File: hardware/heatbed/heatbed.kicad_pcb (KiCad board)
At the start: 2 copper layers, 400 x 400 mm, 0 parts

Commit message: finish board and prod/case files
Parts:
- added J1: Conn_01x01, TestPoint:TestPoint_Pad_D4.0mm, F.Cu at (162.2, 250.3)
- added J2: Conn_01x01, TestPoint:TestPoint_Pad_D4.0mm, F.Cu at (172.3, 250.3)
- added R1: R, Resistor_SMD:R_0805_2012Metric, F.Cu at (167.3, 154.2)
- added R2: R, Resistor_SMD:R_0805_2012Metric, F.Cu at (167.3, 248.8)
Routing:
- net Net-(J1-Pin_1): track 6376.9 -> 0.00 mm
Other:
- board size 400 x 400 mm -> 200 x 200 mm

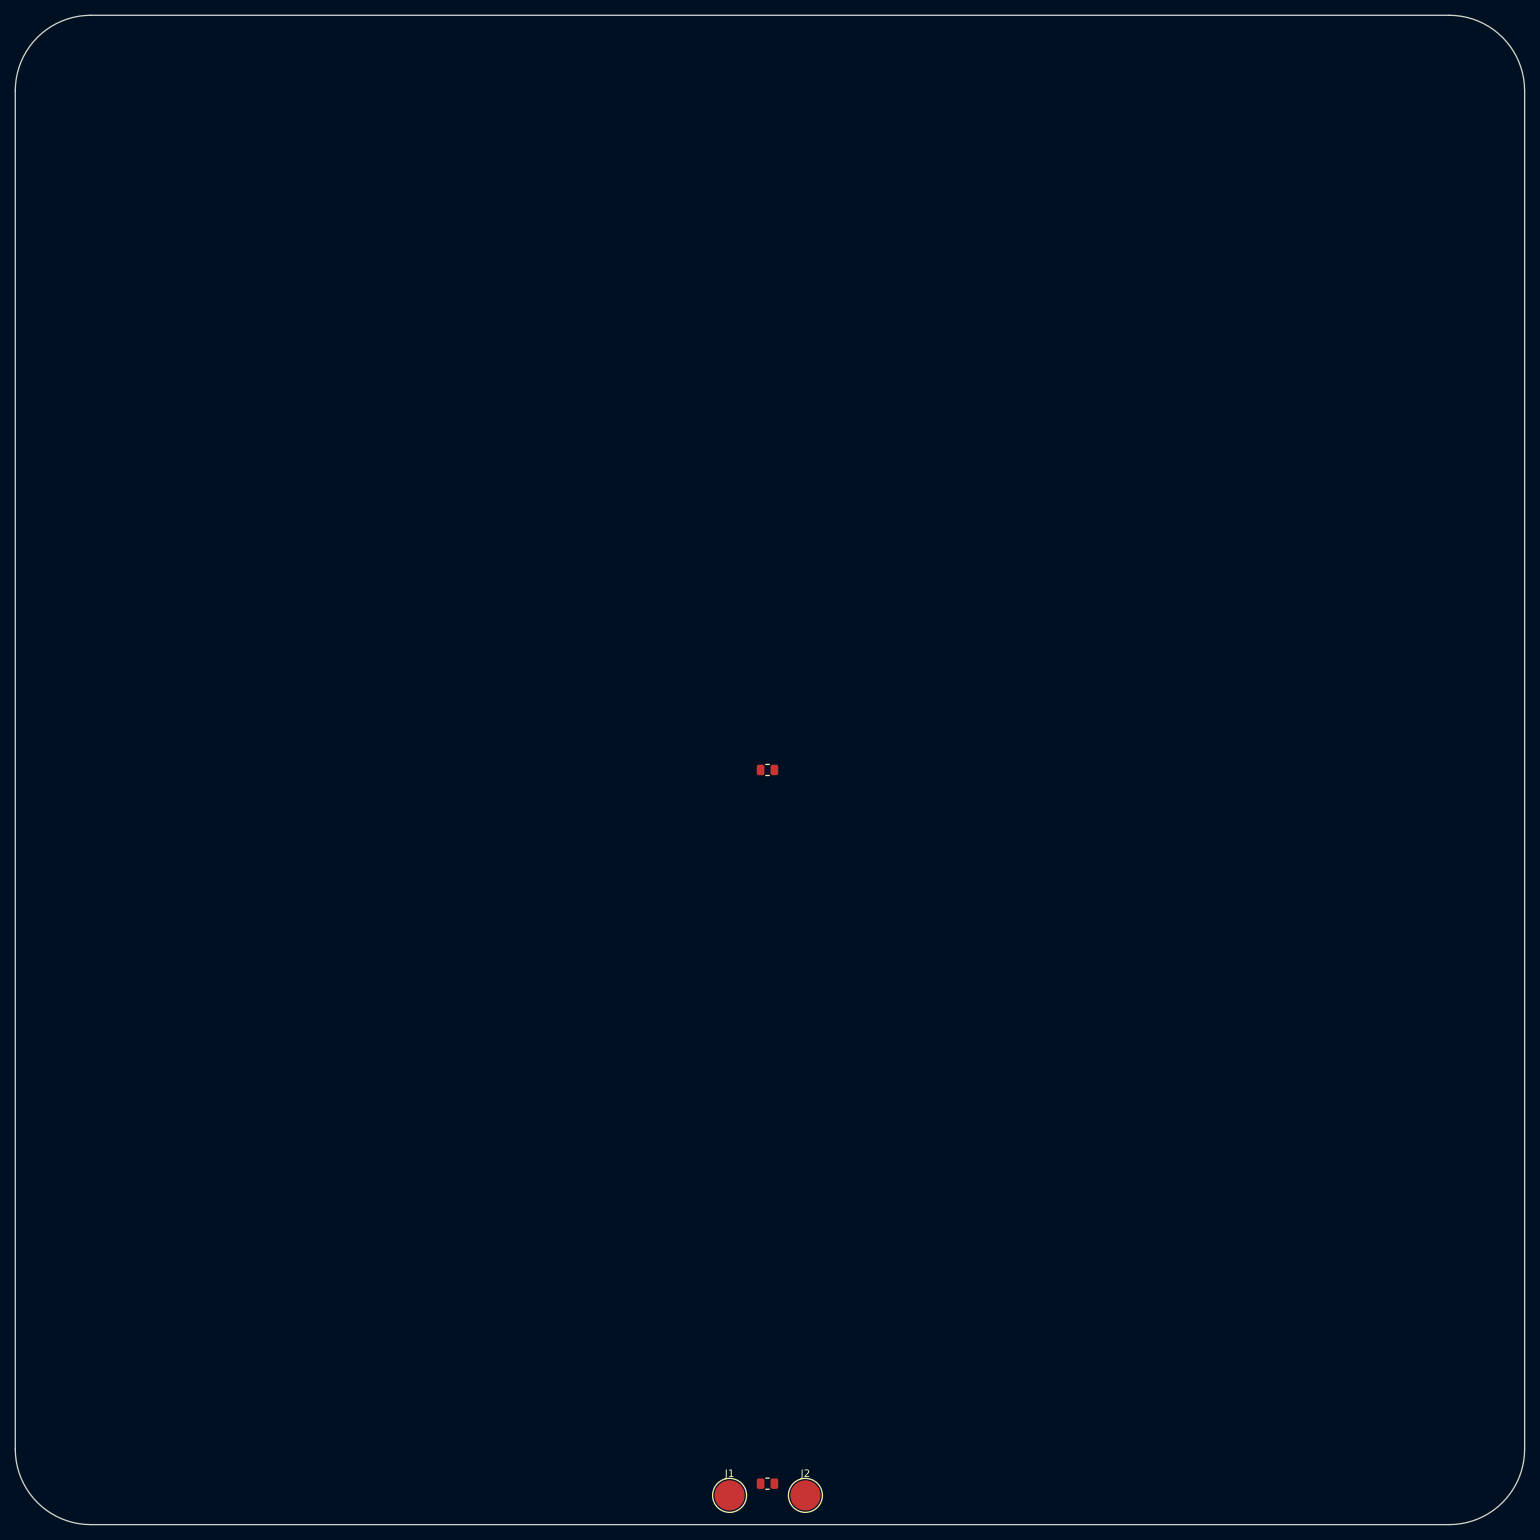
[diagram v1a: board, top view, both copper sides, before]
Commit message: update heatbed
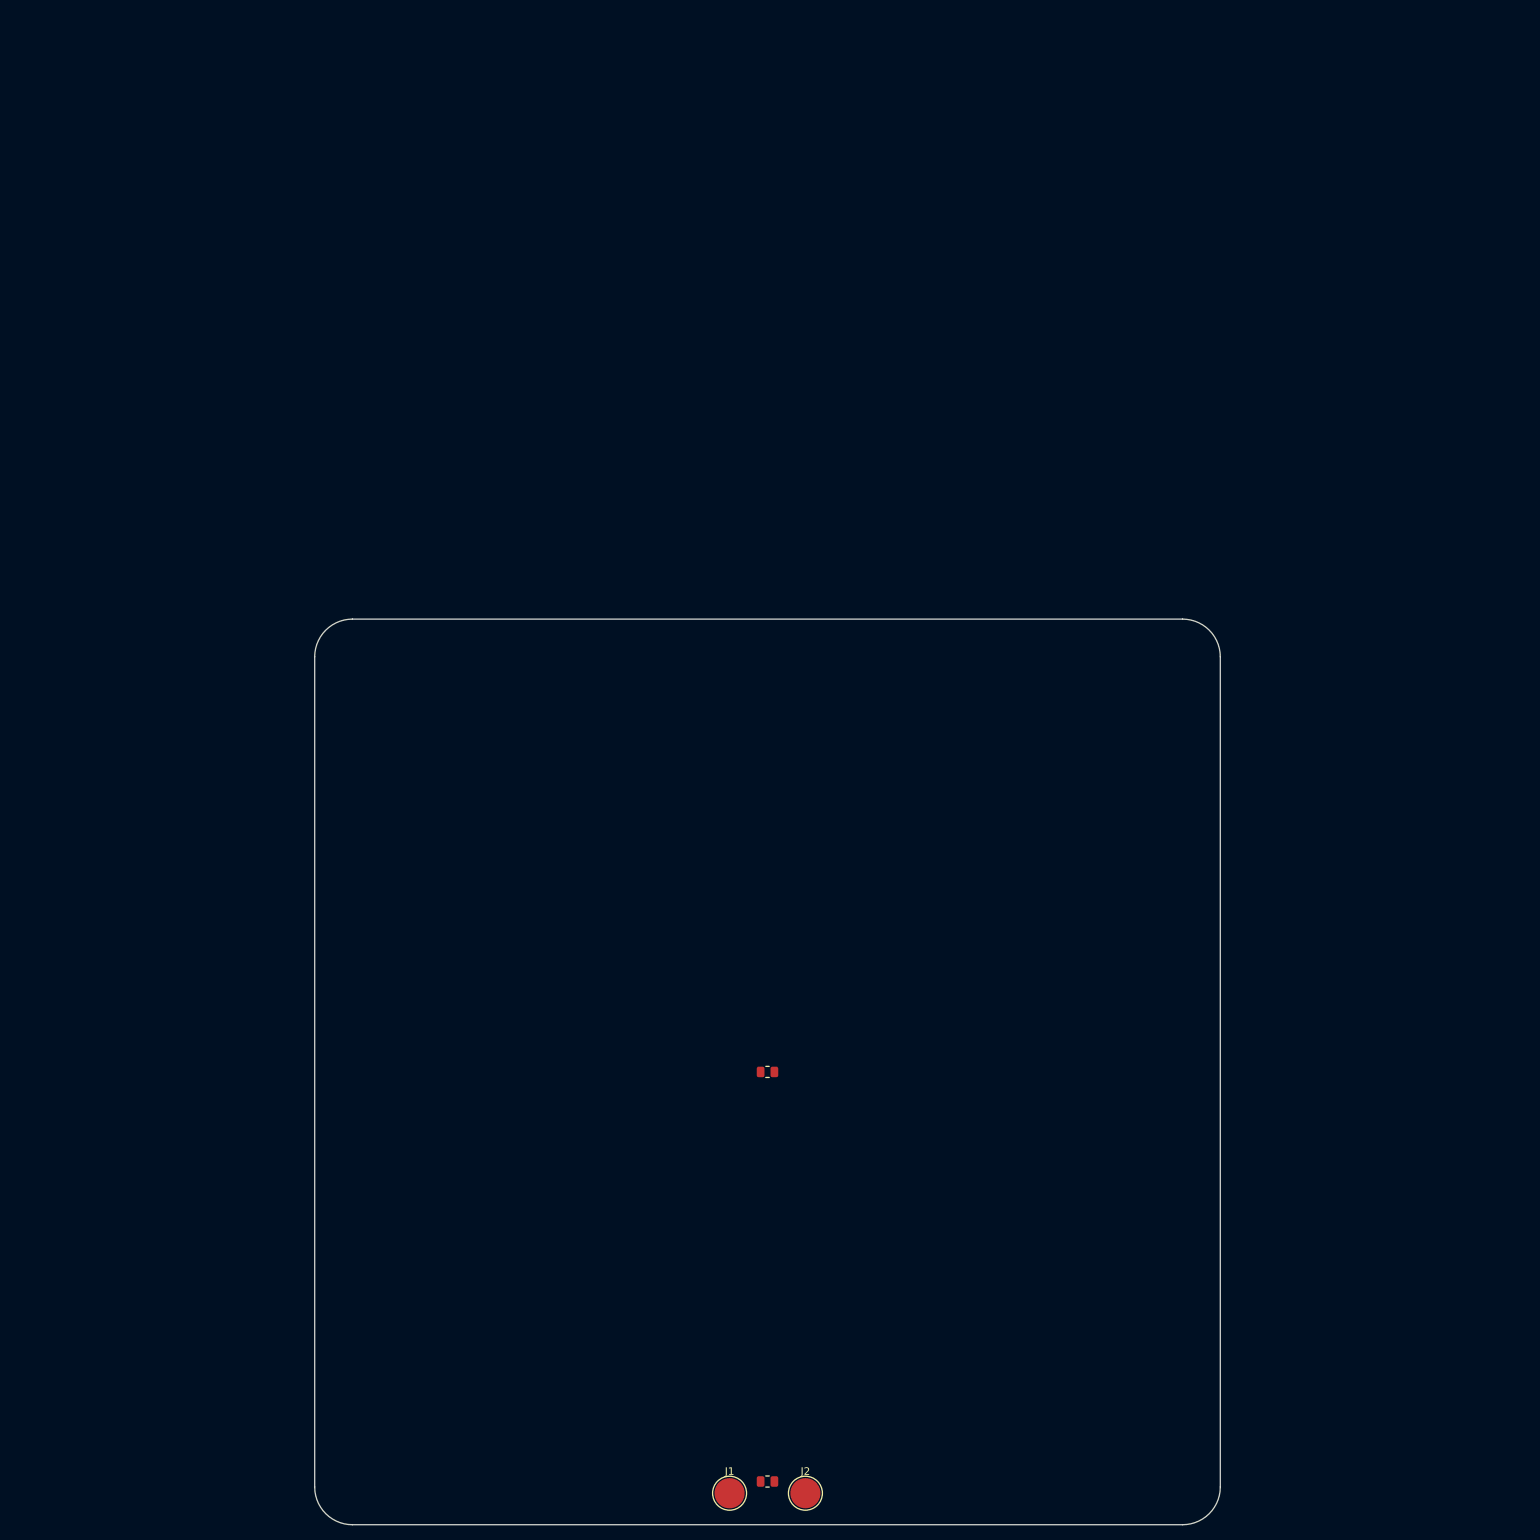
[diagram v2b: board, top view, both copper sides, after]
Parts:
- moved R1 40.0 mm to (167.3, 194.2)
- moved J1 0.29 mm to (162.2, 250.0)
- moved J2 0.29 mm to (172.3, 250.0)
- moved R2 0.29 mm to (167.3, 248.5)
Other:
- board size 200 x 200 mm -> 120 x 120 mm
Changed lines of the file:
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@@
 	(footprint "Resistor_SMD:R_0805_2012Metric"
 		(layer "F.Cu")
-		(at 167.275 248.75 180)
+		(at 167.275 248.46425 180)
 		(descr "Resistor SMD 0805 (2012 Metric), square (rectangular) end terminal, IPC-7351 nominal, (Body size source: IPC-SM-782 page 72, https://www.pcb-3d.com/wordpress/wp-content/uploads/ipc-sm-782a_amendment_1_and_2.pdf), generated with kicad-footprint-generator")
 		(tags "resistor")
@@
 	(footprint "TestPoint:TestPoint_Pad_D4.0mm"
 		(layer "F.Cu")
-		(at 172.3 250.3)
+		(at 172.3 250.01425)
 		(descr "SMD pad as test Point, diameter 4.0mm")
 		(tags "test point SMD pad")
@@
 	(footprint "Resistor_SMD:R_0805_2012Metric"
 		(layer "F.Cu")
-		(at 167.275 154.175 180)
+		(at 167.275 194.1875 180)
 		(descr "Resistor SMD 0805 (2012 Metric), square (rectangular) end terminal, IPC-7351 nominal, (Body size source: IPC-SM-782 page 72, https://www.pcb-3d.com/wordpress/wp-content/uploads/ipc-sm-782a_amendment_1_and_2.pdf), generated with kicad-footprint-generator")
 		(tags "resistor")
@@
 	(footprint "TestPoint:TestPoint_Pad_D4.0mm"
 		(layer "F.Cu")
-		(at 162.25 250.3)
+		(at 162.25 250.01425)
 		(descr "SMD pad as test Point, diameter 4.0mm")
 		(tags "test point SMD pad")
@@
 		(embedded_fonts no)
 	)
+	(gr_line
+		(start 227.275 139.1875)
+		(end 227.275 249.1875)
+		(stroke
+			(width 0.05)
+			(type default)
+		)
+		(layer "Edge.Cuts")
+	)
 	(gr_arc
-		(start 267.6 244.175)
-		(mid 264.671068 251.246068)
-		(end 257.6 254.175)
+		(start 227.275 249.1875)
+		(mid 225.810534 252.723034)
+		(end 222.275 254.1875)
 		(stroke
 			(width 0.05)
@@
 	)
 	(gr_line
-		(start 67.6 244.175)
-		(end 67.6 64.175)
+		(start 107.275 249.1875)
+		(end 107.275 139.1875)
 		(stroke
 			(width 0.05)
@@
 		(layer "Edge.Cuts")
 	)
+	(gr_arc
+		(start 107.275 139.1875)
+		(mid 108.739466 135.651966)
+		(end 112.275 134.1875)
+		(stroke
+			(width 0.05)
+			(type default)
+		)
+		(layer "Edge.Cuts")
+	)
+	(gr_arc
+		(start 222.275 134.1875)
+		(mid 225.810534 135.651966)
+		(end 227.275 139.1875)
+		(stroke
+			(width 0.05)
+			(type default)
+		)
+		(layer "Edge.Cuts")
+	)
+	(gr_arc
+		(start 112.275 254.1875)
+		(mid 108.739466 252.723034)
+		(end 107.275 249.1875)
+		(stroke
+			(width 0.05)
+			(type default)
+		)
+		(layer "Edge.Cuts")
+	)
 	(gr_line
-		(start 267.6 64.175)
-		(end 267.6 244.175)
+		(start 222.275 254.1875)
+		(end 112.275 254.1875)
 		(stroke
 			(width 0.05)
@@
 		(layer "Edge.Cuts")
 	)
-	(gr_arc
-		(start 67.6 64.175)
-		(mid 70.528932 57.103932)
-		(end 77.6 54.175)
-		(stroke
-			(width 0.05)
-			(type default)
-		)
-		(layer "Edge.Cuts")
-	)
-	(gr_arc
-		(start 257.6 54.175)
-		(mid 264.671068 57.103932)
-		(end 267.6 64.175)
-		(stroke
-			(width 0.05)
-			(type default)
-		)
-		(layer "Edge.Cuts")
-	)
 	(gr_line
-		(start 257.6 254.175)
-		(end 77.6 254.175)
-		(stroke
-			(width 0.05)
-			(type default)
-		)
-		(layer "Edge.Cuts")
-	)
-	(gr_arc
-		(start 77.6 254.175)
-		(mid 70.528932 251.246068)
-		(end 67.6 244.175)
-		(stroke
-			(width 0.05)
-			(type default)
-		)
-		(layer "Edge.Cuts")
-	)
-	(gr_line
-		(start 77.6 54.175)
-		(end 257.6 54.175)
-		(stroke
-			(width 0.05)
+		(start 112.275 134.1875)
+		(end 222.275 134.1875)
+		(stroke
+			(width 0.05)
